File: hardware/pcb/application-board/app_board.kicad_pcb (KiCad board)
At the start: 2 copper layers, 276 x 45 mm, 80 parts, among them J101 Conn_01x04_Socket, J102 Conn_02x08_Top_Bottom, J103 Conn_01x04_Socket, J201 DISP_PCB x40 FPC, Q201 DMG2302U, Q202 DMG2301L

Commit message: start layout of application board
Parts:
- added C201: 100nF, Capacitor_SMD:C_0805_2012Metric_Pad1.18x1.45mm_HandSolder, F.Cu at (121.6, 183.9)
- added H203: PWR_555, Connector_Pin:Pin_D0.7mm_L6.5mm_W1.8mm_FlatFork, F.Cu at (113.6, 177.6)
- added H204: TR, Connector_Pin:Pin_D0.7mm_L6.5mm_W1.8mm_FlatFork, F.Cu at (113.6, 181.0)
- added H205: CV, Connector_Pin:Pin_D0.7mm_L6.5mm_W1.8mm_FlatFork, F.Cu at (113.6, 184.5)
- added H206: R, Connector_Pin:Pin_D0.7mm_L6.5mm_W1.8mm_FlatFork, F.Cu at (113.6, 187.9)
- added H207: Q, Connector_Pin:Pin_D0.7mm_L6.5mm_W1.8mm_FlatFork, F.Cu at (117.4, 177.6)
- added H208: DIS, Connector_Pin:Pin_D0.7mm_L6.5mm_W1.8mm_FlatFork, F.Cu at (117.4, 181.0)
- added H209: THR, Connector_Pin:Pin_D0.7mm_L6.5mm_W1.8mm_FlatFork, F.Cu at (117.4, 184.5)
- added U201: Unused 555, Package_SO:SOIC-8_3.9x4.9mm_P1.27mm, F.Cu at (123.5, 179.2)
- moved JP219 93.6 mm to (228.8, 35.1)
- moved JP220 90.0 mm to (229.1, 42.9)
- moved JP213 88.3 mm to (208.9, 34.8)
- moved JP207 87.2 mm to (194.6, 33.5)
- moved JP221 86.6 mm to (229.0, 50.3)
- moved JP201 85.4 mm to (172.9, 34.0)
- moved JP222 85.3 mm to (230.4, 56.0)
- moved JP214 84.4 mm to (209.7, 42.7)
- moved JP223 82.8 mm to (230.7, 62.8)
- moved JP208 82.7 mm to (194.4, 41.6)
- moved JP215 80.7 mm to (210.8, 50.5)
- moved JP224 79.8 mm to (231.2, 70.2)
- moved JP209 78.5 mm to (194.9, 49.5)
- moved JP216 77.9 mm to (210.8, 57.0)
- moved JP202 77.0 mm to (171.0, 46.0)
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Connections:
- J201 pad 1: GND -> +5V
- J201 pad 11: GND -> Net-(J201-Pin_11)
- J201 pad 15: Net-(J201-Pin_15) -> GND
- J201 pad 16: GND -> Net-(J201-Pin_16)
- J201 pad 2: /Z88R Connection/ENABLE_APP_BOARD -> +5V
- J201 pad 25: Net-(J201-Pin_25) -> GND
- J201 pad 26: GND -> Net-(J201-Pin_26)
- J201 pad 3: Net-(J201-Pin_3) -> +5V
- J201 pad 30: Net-(J201-Pin_30) -> GND
- J201 pad 33: Net-(J201-Pin_33) -> GND
- J201 pad 38: +5V -> Net-(J201-Pin_38)
- J201 pad 39: +5V -> /Z88R Connection/ENABLE_APP_BOARD
- J201 pad 40: +5V -> GND
- J201 pad 8: GND -> Net-(J201-Pin_8)
- JP201 pad 1: Net-(J201-Pin_36) -> Net-(J201-Pin_5)
- JP202 pad 1: Net-(J201-Pin_35) -> Net-(J201-Pin_6)
- JP203 pad 1: Net-(J201-Pin_34) -> Net-(J201-Pin_7)
- JP204 pad 1: Net-(J201-Pin_33) -> Net-(J201-Pin_8)
- JP205 pad 1: Net-(J201-Pin_32) -> Net-(J201-Pin_9)
- JP206 pad 1: Net-(J201-Pin_31) -> Net-(J201-Pin_10)
- JP207 pad 1: Net-(J201-Pin_30) -> Net-(J201-Pin_11)
- JP208 pad 1: Net-(J201-Pin_29) -> Net-(J201-Pin_12)
- JP209 pad 1: Net-(J201-Pin_28) -> Net-(J201-Pin_13)
- JP210 pad 1: Net-(J201-Pin_27) -> Net-(J201-Pin_14)
- JP211 pad 1: Net-(J201-Pin_25) -> Net-(J201-Pin_16)
- JP212 pad 1: Net-(J201-Pin_24) -> Net-(J201-Pin_17)
- JP213 pad 1: Net-(J201-Pin_23) -> Net-(J201-Pin_18)
- JP214 pad 1: Net-(J201-Pin_22) -> Net-(J201-Pin_19)
- JP215 pad 1: Net-(J201-Pin_21) -> Net-(J201-Pin_20)
- JP216 pad 1: Net-(J201-Pin_20) -> Net-(J201-Pin_21)
- JP217 pad 1: Net-(J201-Pin_19) -> Net-(J201-Pin_22)
- JP218 pad 1: Net-(J201-Pin_18) -> Net-(J201-Pin_23)
- JP219 pad 1: Net-(J201-Pin_17) -> Net-(J201-Pin_24)
- JP220 pad 1: Net-(J201-Pin_15) -> Net-(J201-Pin_26)
- JP221 pad 1: Net-(J201-Pin_14) -> Net-(J201-Pin_27)
- JP222 pad 1: Net-(J201-Pin_13) -> Net-(J201-Pin_28)
- JP223 pad 1: Net-(J201-Pin_12) -> Net-(J201-Pin_29)
- JP224 pad 1: Net-(J201-Pin_10) -> Net-(J201-Pin_31)
- JP225 pad 1: Net-(J201-Pin_9) -> Net-(J201-Pin_32)
- JP226 pad 1: Net-(J201-Pin_7) -> Net-(J201-Pin_34)
- JP227 pad 1: Net-(J201-Pin_6) -> Net-(J201-Pin_35)
- JP228 pad 1: Net-(J201-Pin_5) -> Net-(J201-Pin_36)
- JP229 pad 1: Net-(J201-Pin_3) -> Net-(J201-Pin_38)
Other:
- board text added: "Note how this connector is arranged relative to the one on the main board. They are facing each other, so pin 1 on the main board (GND) is on the right side, and that matches up with pin 40 on this board. So pin 40 on this side is GND. The sequence of pins is essentially inverted so a straight cable takes the signals out of one connector into the other."
- board text removed: "Assume a 100mm flexicable. Need to measure the exact position of this connector, based on the one on the main board."

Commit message: more layout work
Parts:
- moved JP219 115.4 mm to (226.1, 150.5)
- moved JP213 113.1 mm to (199.1, 147.5), turned to 180 degrees
- moved JP220 107.6 mm to (229.7, 150.5)
- moved JP214 105.0 mm to (202.7, 147.5)
- moved JP221 100.2 mm to (233.8, 150.4)
- moved JP215 97.1 mm to (206.4, 147.5), turned to 180 degrees
- moved JP222 94.5 mm to (237.6, 150.3)
- moved JP223 90.9 mm to (227.9, 153.6)
- moved JP216 90.5 mm to (210.0, 147.5)
- moved JP201 85.8 mm to (199.2, 115.7)
- moved JP217 85.2 mm to (213.7, 147.5), turned to 180 degrees
- moved JP224 83.4 mm to (232.3, 153.5)
- moved JP207 82.8 mm to (205.3, 115.7)
- moved JP218 78.8 mm to (217.3, 147.5)
- moved JP202 78.7 mm to (199.0, 119.6)
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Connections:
- net Net-(A101-VSYS) renamed /PICO_PWR
- net Net-(Q201-D) renamed /Z88R Connection/PCHAN_GATE
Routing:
- net 5V_SWITCHED: track 0.00 -> 147.4 mm, vias 0 -> 5
- net PICO1_3V3: track 0.00 -> 130.5 mm, vias 0 -> 3
- net Net-(A101-GPIO2): track 0.00 -> 107.0 mm, vias 0 -> 3
- net Net-(A101-GPIO3): track 0.00 -> 106.6 mm, vias 0 -> 4
- net /PICO_PWR: track 0.00 -> 104.7 mm, vias 0 -> 7
- net PICO1_I2C_CLK: track 0.00 -> 102.5 mm, vias 0 -> 3
- net Net-(A101-GPIO9): track 0.00 -> 101.8 mm, vias 0 -> 3
- net Net-(A101-GPIO8): track 0.00 -> 101.2 mm, vias 0 -> 3
- net Net-(A101-GPIO7): track 0.00 -> 100.2 mm, vias 0 -> 3
- net Net-(A101-GPIO6): track 0.00 -> 99.6 mm, vias 0 -> 3
- net Net-(A101-GPIO10): track 0.00 -> 97.9 mm, vias 0 -> 3
- net Net-(A101-GPIO28_ADC2): track 0.00 -> 96.8 mm, vias 0 -> 3
- net PICO1_I2C_DAT: track 0.00 -> 96.6 mm, vias 0 -> 3
- net Net-(A101-GPIO26_ADC0): track 0.00 -> 95.8 mm, vias 0 -> 3
- net Net-(A101-GPIO27_ADC1): track 0.00 -> 94.9 mm, vias 0 -> 3
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
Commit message: more layout work
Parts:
- moved JP224 11.5 mm to (227.8, 142.9)
- moved JP223 11.4 mm to (223.8, 142.9), turned to 180 degrees
- moved JP213 9.99 mm to (189.4, 150.2)
- moved JP214 9.99 mm to (193.1, 150.2)
- moved JP215 9.99 mm to (196.8, 150.2)
- moved JP216 9.99 mm to (200.4, 150.2)
- moved JP217 9.99 mm to (204.1, 150.2)
- moved JP218 9.99 mm to (207.7, 150.2)
- moved JP227 8.44 mm to (238.9, 143.1), turned to 180 degrees
- moved JP229 7.12 mm to (242.1, 135.8), turned to -90 degrees
- moved JP226 6.86 mm to (235.4, 142.9)
- moved JP228 5.16 mm to (240.6, 139.7), turned to -90 degrees
- moved JP225 1.01 mm to (231.7, 142.9), turned to 180 degrees
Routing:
- net CM4_GPIO2_SDA1: track 0.00 -> 187.1 mm, vias 0 -> 5
- net CM4_GPIO3_SCL1: track 0.00 -> 183.1 mm, vias 0 -> 7
- net CM4_GPIO19_PWM: track 0.00 -> 177.6 mm, vias 0 -> 5
- net PICO2_GPIO3: track 35.2 -> 135.7 mm, vias 2 -> 4
- net PICO2_GPIO4: track 34.9 -> 125.0 mm, vias 2 -> 4
- net CM4_TX_TO_PICO1: track 0.00 -> 90.1 mm, vias 0 -> 4
- net PICO2_GPIO0: track 44.5 -> 131.2 mm, vias 2 -> 4
- net SUPPORT_PICO_TX_TO_DISP: track 0.00 -> 83.0 mm, vias 0 -> 4
- net PICO2_3V3: track 22.2 -> 98.5 mm, vias 1 -> 2
- net PICO2_GPIO1: track 45.2 -> 120.2 mm, vias 2 -> 4
- net PICO2_GPIO5: track 28.3 -> 102.8 mm, vias 2 -> 4
- net SUPPORT_PICO_RX_FROM_DISP: track 0.00 -> 69.7 mm, vias 0 -> 4
- net Net-(A102-GPIO9): track 0.00 -> 69.6 mm, vias 0 -> 2
- net Net-(A102-GPIO28_ADC2): track 0.00 -> 69.0 mm, vias 0 -> 2
- net PICO2_GPIO7: track 25.3 -> 93.2 mm, vias 2 -> 6
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
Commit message: more layout work
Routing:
- net PICO1_UART_TX: track 0.00 -> 215.7 mm, vias 0 -> 6
- net PICO1_UART_RX: track 0.00 -> 201.4 mm, vias 0 -> 6
- net DISPLAY_PICO2_SWD_IO: track 0.00 -> 99.2 mm, vias 0 -> 4
- net DISPLAY_PICO2_SWD_CLK: track 0.00 -> 91.7 mm, vias 0 -> 4
- net PICO_SEL: track 0.00 -> 63.9 mm, vias 0 -> 4
- net Net-(J201-Pin_18): track 0.00 -> 51.7 mm, vias 0 -> 6
- net Net-(J201-Pin_19): track 0.00 -> 48.7 mm, vias 0 -> 2
- net Net-(J201-Pin_20): track 0.00 -> 44.8 mm, vias 0 -> 4
- net Net-(J201-Pin_21): track 0.00 -> 43.1 mm, vias 0 -> 4
- net Net-(J201-Pin_22): track 0.00 -> 38.7 mm, vias 0 -> 4
- net Net-(J201-Pin_23): track 0.00 -> 36.9 mm, vias 0 -> 4
- net Net-(J201-Pin_14): track 0.00 -> 32.8 mm, vias 0 -> 4
- net Net-(J201-Pin_28): track 0.00 -> 26.3 mm, vias 0 -> 2
- net Net-(J201-Pin_16): track 0.00 -> 25.8 mm, vias 0 -> 4
- net Net-(J201-Pin_17): track 0.00 -> 25.0 mm, vias 0 -> 2
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
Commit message: layout complete, first draft, needs tidying
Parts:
- moved C201 80.1 mm to (76.8, 117.6)
- moved U201 71.3 mm to (80.1, 122.7)
- moved H205 56.5 mm to (83.9, 136.4)
- moved H203 56.5 mm to (83.9, 129.6)
- moved H204 56.5 mm to (83.9, 133.0)
- moved H206 56.5 mm to (83.9, 139.9)
- moved H209 47.3 mm to (84.0, 150.9)
- moved H207 47.3 mm to (84.0, 144.1)
- moved H208 47.3 mm to (84.0, 147.5)
- moved H201 7.54 mm to (77.3, 134.1)
- moved H202 7.54 mm to (77.2, 142.2)
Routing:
- net +5V: track 47.9 -> 227.5 mm, vias 4 -> 7
- net DISPLAY_PICO1_SWD_IO: track 0.00 -> 126.5 mm, vias 0 -> 2
- net DISPLAY_PICO1_SWD_CLK: track 0.00 -> 121.2 mm, vias 0 -> 2
- net PICO_SEL: track 63.9 -> 176.7 mm, vias 4 -> 10
- net CM4_RX_FROM_PICO1: track 0.00 -> 86.7 mm, vias 0 -> 6
- net Net-(J201-Pin_11): track 0.00 -> 37.8 mm, vias 0 -> 4
- net Net-(J201-Pin_5): track 0.00 -> 35.4 mm, vias 0 -> 4
- net GND: track 31.3 -> 66.1 mm, vias 19 -> 26
- net Net-(J201-Pin_12): track 0.00 -> 34.7 mm, vias 0 -> 4
- net Net-(U201-DIS): track 0.00 -> 34.4 mm, vias 0 -> 3
- net Net-(U201-THR): track 0.00 -> 32.3 mm, vias 0 -> 1
- net Net-(J201-Pin_6): track 0.00 -> 32.0 mm, vias 0 -> 4
- net Net-(J201-Pin_13): track 0.00 -> 31.8 mm, vias 0 -> 4
- net Net-(J201-Pin_7): track 0.00 -> 30.9 mm, vias 0 -> 4
- net Net-(U201-Q): track 0.00 -> 28.0 mm, vias 0 -> 3
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
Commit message: fab1.0 off to JLC
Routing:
- net +5V: track 227.5 -> 222.4 mm

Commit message: start v1.1, missed some tidyups and a label
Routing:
- net DISPLAY_PICO2_SWD_IO: track 99.2 -> 97.4 mm
- net GND: track 66.1 -> 64.8 mm
- net Net-(A102-GPIO15): track 16.9 -> 15.9 mm
- net +5V: track 222.4 -> 221.6 mm
- net PICO1_UART_RX: track 201.6 -> 200.8 mm
- net Net-(A101-GPIO10): track 97.9 -> 97.2 mm
- net PICO_SEL: track 176.7 -> 176.2 mm
- net Net-(A102-GPIO11): track 43.1 -> 42.5 mm
- net PICO2_GPIO2: track 115.6 -> 115.1 mm
- net DISPLAY_PICO1_SWD_IO: track 126.5 -> 125.9 mm
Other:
- board text added: "Z88 Recreation Application Board v1.1 https://github.com/derekfountain/z88-recreation"

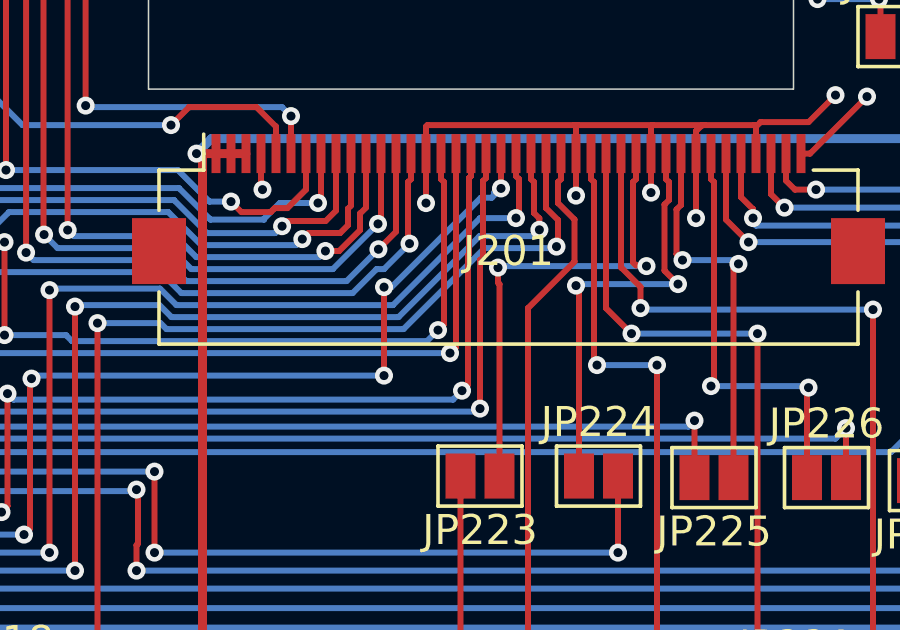
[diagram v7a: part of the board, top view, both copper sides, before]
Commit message: start v1.1 pcb, add FPC connector label
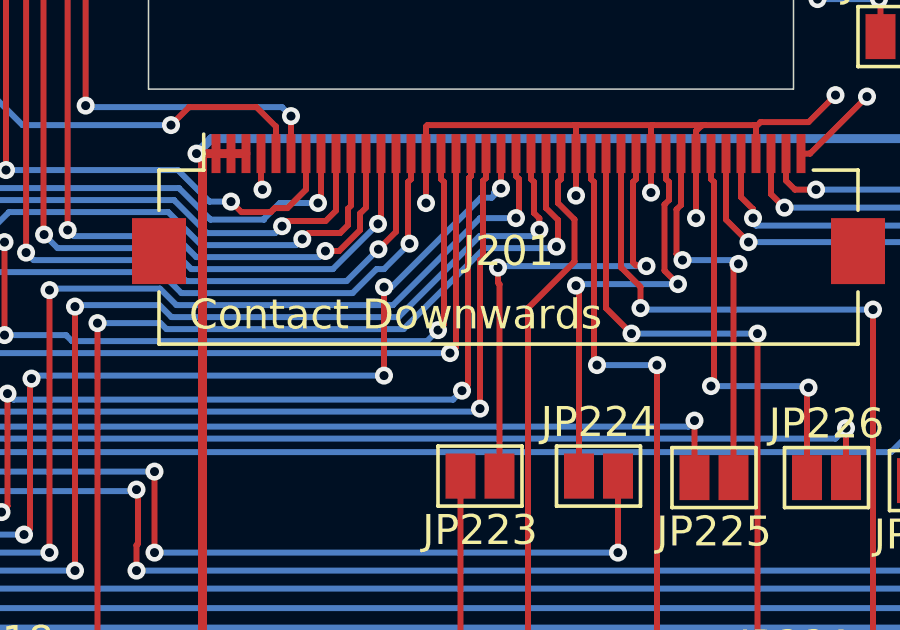
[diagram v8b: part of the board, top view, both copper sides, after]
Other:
- board text added: "Contact Downwards"
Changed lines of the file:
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@@
+		)
+	)
+	(gr_text "Contact Downwards"
+		(at 214.15 138.1 0)
+		(layer "F.SilkS")
+		(effects
+			(font
+				(size 1 1)
+				(thickness 0.1)
+			)
+			(justify left bottom)
 		)
 	)
